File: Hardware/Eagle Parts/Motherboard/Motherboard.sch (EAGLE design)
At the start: 30 parts, among them J1 U.FL, U1 MK10DN512ZVLL10, U4 MPL3115A2LGA8, U5 ATMEGA8U2AU, U6 MPL115A

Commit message: Moved things into separate pages
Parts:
- removed J1: U.FL, SparkFun-Connectors:U.FL
- removed U$10, U$11, U$12, U$13, U$14, U$15, U$3, U$5, U$6, U$7, U$8, U$9: MAX3077, MAX3077:MAX3077
- removed U$24: TB60050685100, harting-scsi:TB60050685100
- removed U2: (no value), adafruit:GPS_FGPMMOPA6H
- removed U3: (no value), SparkFun-Sensors:MPU-9150QFN-24-NP
- removed U4: MPL3115A2LGA8, SparkFun-Sensors:MPL3115A2LGA8
- removed U6: MPL115A, SparkFun-Sensors:MPL115A
- added J2: U.FL, SparkFun-Connectors:U.FL
- added U$25, U$26, U$27, U$28, U$29, U$30, U$31, U$32, U$33, U$34, U$35, U$4: MAX3077, MAX3077:MAX3077
- added U$36: TB60050685100, harting-scsi:TB60050685100
- added U10: MPL115A, SparkFun-Sensors:MPL115A
- added U7: (no value), adafruit:GPS_FGPMMOPA6H
- added U8: (no value), SparkFun-Sensors:MPU-9150QFN-24-NP
- added U9: MPL3115A2LGA8, SparkFun-Sensors:MPL3115A2LGA8
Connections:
- net 10_RX+: now also U$26.A, U$36.39; no longer U$24.39, U$6.A
- net 10_RX-: now also U$26.B, U$36.40; no longer U$24.40, U$6.B
- net 10_TX+: now also U$26.Y, U$36.37; no longer U$24.37, U$6.Y
- net 10_TX-: now also U$26.Z, U$36.38; no longer U$24.38, U$6.Z
- net 11_RX+: now also U$25.A, U$36.43; no longer U$24.43, U$5.A
- net 11_RX-: now also U$25.B, U$36.44; no longer U$24.44, U$5.B
- net 11_TX+: now also U$25.Y, U$36.41; no longer U$24.41, U$5.Y
- net 11_TX-: now also U$25.Z, U$36.42; no longer U$24.42, U$5.Z
- net 12_RX+: now also U$36.47, U$4.A; no longer U$24.47, U$3.A
- net 12_RX-: now also U$36.48, U$4.B; no longer U$24.48, U$3.B
- net 12_TX+: now also U$36.45, U$4.Y; no longer U$24.45, U$3.Y
- net 12_TX-: now also U$36.46, U$4.Z; no longer U$24.46, U$3.Z
- net 1_RX+: now also U$29.A, U$36.3; no longer U$24.3, U$9.A
- net 1_RX-: now also U$29.B, U$36.4; no longer U$24.4, U$9.B
- net 1_TX+: now also U$29.Y, U$36.1; no longer U$24.1, U$9.Y
- net 1_TX-: now also U$29.Z, U$36.2; no longer U$24.2, U$9.Z
- net 2_RX+: now also U$31.A, U$36.7; no longer U$11.A, U$24.7
- net 2_RX-: now also U$31.B, U$36.8; no longer U$11.B, U$24.8
- net 2_TX+: now also U$31.Y, U$36.5; no longer U$11.Y, U$24.5
- net 2_TX-: now also U$31.Z, U$36.6; no longer U$11.Z, U$24.6
- net 3_RX+: now also U$32.A, U$36.11; no longer U$12.A, U$24.11
- net 3_RX-: now also U$32.B, U$36.12; no longer U$12.B, U$24.12
- net 3_TX+: now also U$32.Y, U$36.9; no longer U$12.Y, U$24.9
- net 3_TX-: now also U$32.Z, U$36.10; no longer U$12.Z, U$24.10
- net 4_RX+: now also U$33.A, U$36.15; no longer U$13.A, U$24.15
- net 4_RX-: now also U$33.B, U$36.16; no longer U$13.B, U$24.16
- net 4_TX+: now also U$33.Y, U$36.13; no longer U$13.Y, U$24.13
- net 4_TX-: now also U$33.Z, U$36.14; no longer U$13.Z, U$24.14
- net 5_RX+: now also U$34.A, U$36.19; no longer U$14.A, U$24.19
- net 5_RX-: now also U$34.B, U$36.20; no longer U$14.B, U$24.20
- net 5_TX+: now also U$34.Y, U$36.17; no longer U$14.Y, U$24.17
- net 5_TX-: now also U$34.Z, U$36.18; no longer U$14.Z, U$24.18
- net 6_RX+: now also U$35.A, U$36.23; no longer U$15.A, U$24.23
- net 6_RX-: now also U$35.B, U$36.24; no longer U$15.B, U$24.24
- net 6_TX+: now also U$35.Y, U$36.21; no longer U$15.Y, U$24.21
- net 6_TX-: now also U$35.Z, U$36.22; no longer U$15.Z, U$24.22
- net 7_RX+: now also U$30.A, U$36.27; no longer U$10.A, U$24.27
- net 7_RX-: now also U$30.B, U$36.28; no longer U$10.B, U$24.28
- net 7_TX+: now also U$30.Y, U$36.25; no longer U$10.Y, U$24.25
- net 7_TX-: now also U$30.Z, U$36.26; no longer U$10.Z, U$24.26
- net 8_RX+: now also U$28.A, U$36.31; no longer U$24.31, U$8.A
- net 8_RX-: now also U$28.B, U$36.32; no longer U$24.32, U$8.B
- net 8_TX+: now also U$28.Y, U$36.29; no longer U$24.29, U$8.Y
- net 8_TX-: now also U$28.Z, U$36.30; no longer U$24.30, U$8.Z
- net 9_RX+: now also U$27.A, U$36.35; no longer U$24.35, U$7.A
- net 9_RX-: now also U$27.B, U$36.36; no longer U$24.36, U$7.B
- net 9_TX+: now also U$27.Y, U$36.33; no longer U$24.33, U$7.Y
- net 9_TX-: now also U$27.Z, U$36.34; no longer U$24.34, U$7.Z
- net GND: now also U$25.GND, U$26.GND, U$27.GND, U$28.GND, U$29.GND, U$30.GND, U$31.GND, U$32.GND, U$33.GND, U$34.GND, U$35.GND, U$4.GND; no longer U$10.GND, U$11.GND, U$12.GND, U$13.GND, U$14.GND, U$15.GND, U$3.GND, U$5.GND, U$6.GND, U$7.GND, U$8.GND, U$9.GND

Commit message: Wired Sensor Grounds, Created RS Internal Page
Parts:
- removed U$16, U$17, U$18, U$19, U$20, U$21, U$22, U$23: MAX3077, MAX3077:MAX3077
- added U$10, U$11, U$3, U$5, U$6, U$7, U$8, U$9: MAX3077, MAX3077:MAX3077
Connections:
- net GND: now also U10.GND, U7.GND@1, U7.GND@2, U7.GND@3, U7.GND@4, U8.GND@15, U8.GND@17, U8.GND@18, U9.GND
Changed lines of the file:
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@@
 <part name="U$1" library="w5500_wiznet" deviceset="W5500" device=""/>
 <part name="U$2" library="SPBT2632C2A" deviceset="SPBT2632C2A" device=""/>
-<part name="U$16" library="MAX3077" deviceset="MAX3077" device=""/>
-<part name="U$17" library="MAX3077" deviceset="MAX3077" device=""/>
-<part name="U$18" library="MAX3077" deviceset="MAX3077" device=""/>
-<part name="U$19" library="MAX3077" deviceset="MAX3077" device=""/>
-<part name="U$20" library="MAX3077" deviceset="MAX3077" device=""/>
-<part name="U$21" library="MAX3077" deviceset="MAX3077" device=""/>
-<part name="U$22" library="MAX3077" deviceset="MAX3077" device=""/>
-<part name="U$23" library="MAX3077" deviceset="MAX3077" device=""/>
 <part name="GND1" library="supply1" deviceset="GND" device=""/>
 <part name="U$4" library="MAX3077" deviceset="MAX3077" device=""/>
@@
 <part name="J2" library="SparkFun-Connectors" deviceset="U.FL" device=""/>
 <part name="U10" library="SparkFun-Sensors" deviceset="MPL115A" device=""/>
+<part name="GND2" library="supply1" deviceset="GND" device=""/>
+<part name="GND3" library="supply1" deviceset="GND" device=""/>
+<part name="GND4" library="supply1" deviceset="GND" device=""/>
+<part name="GND5" library="supply1" deviceset="GND" device=""/>
+<part name="GND6" library="supply1" deviceset="GND" device=""/>
+<part name="GND7" library="supply1" deviceset="GND" device=""/>
+<part name="GND8" library="supply1" deviceset="GND" device=""/>
+<part name="U$3" library="MAX3077" deviceset="MAX3077" device=""/>
+<part name="U$5" library="MAX3077" deviceset="MAX3077" device=""/>
+<part name="U$6" library="MAX3077" deviceset="MAX3077" device=""/>
+<part name="U$7" library="MAX3077" deviceset="MAX3077" device=""/>
+<part name="U$8" library="MAX3077" deviceset="MAX3077" device=""/>
+<part name="U$9" library="MAX3077" deviceset="MAX3077" device=""/>
+<part name="U$10" library="MAX3077" deviceset="MAX3077" device=""/>
+<part name="U$11" library="MAX3077" deviceset="MAX3077" device=""/>
 </parts>
 <sheets>
@@
 <text x="-93.98" y="7.62" size="5.08" layer="91">TCP/Eth</text>
 <text x="-91.44" y="-91.44" size="5.08" layer="91">Bluetooth</text>
-<text x="-2.54" y="-63.5" size="5.08" layer="91">RS-485</text>
 </plain>
 <instances>
@@
 <instance part="U$1" gate="G$1" x="-96.52" y="-60.96"/>
 <instance part="U$2" gate="G$1" x="-73.66" y="-116.84"/>
-<instance part="U$16" gate="G$1" x="10.16" y="-76.2"/>
-<instance part="U$17" gate="G$1" x="53.34" y="-73.66"/>
-<instance part="U$18" gate="G$1" x="91.44" y="-73.66"/>
-<instance part="U$19" gate="G$1" x="132.08" y="-73.66"/>
-<instance part="U$20" gate="G$1" x="175.26" y="-71.12"/>
-<instance part="U$21" gate="G$1" x="215.9" y="-71.12"/>
-<instance part="U$22" gate="G$1" x="172.72" y="-114.3"/>
-<instance part="U$23" gate="G$1" x="213.36" y="-114.3"/>
 <instance part="GND1" gate="1" x="-27.94" y="114.3" rot="R270"/>
 </instances>
@@
 </sheet>
 <sheet>
-<description>RS-485</description>
+<description>RS-485 External</description>
 <plain>
 <text x="88.9" y="104.14" size="5.08" layer="91">Ribbon Cable</text>
@@
 </sheet>
 <sheet>
-<description>Sensors</description>
+<description>RS-485 Internal</description>
 <plain>
-<text x="-15.24" y="58.42" size="12.7" layer="91" align="center">GPS</text>
-<text x="35.56" y="58.42" size="12.7" layer="91" align="center">IMU</text>
-<text x="-22.86" y="-17.78" size="5.08" layer="91" align="center">Altimeter</text>
-<text x="5.08" y="-20.32" size="5.08" layer="91">Barometer</text>
+<text x="-116.84" y="30.48" size="5.08" layer="91">RS-485</text>
 </plain>
 <instances>
-<instance part="U7" gate="G$1" x="-20.32" y="20.32"/>
-<instance part="U8" gate="G$1" x="35.56" y="22.86"/>
-<instance part="U9" gate="G$1" x="-20.32" y="-33.02"/>
-<instance part="J2" gate="G$1" x="-50.8" y="38.1"/>
-<instance part="U10" gate="G$1" x="20.32" y="-33.02"/>
+<instance part="U$3" gate="G$1" x="-104.14" y="17.78"/>
+<instance part="U$5" gate="G$1" x="-60.96" y="20.32"/>
+<instance part="U$6" gate="G$1" x="-22.86" y="20.32"/>
+<instance part="U$7" gate="G$1" x="17.78" y="20.32"/>
+<instance part="U$8" gate="G$1" x="60.96" y="22.86"/>
+<instance part="U$9" gate="G$1" x="101.6" y="22.86"/>
+<instance part="U$10" gate="G$1" x="58.42" y="-20.32"/>
+<instance part="U$11" gate="G$1" x="99.06" y="-20.32"/>
 </instances>
 <busses>
@@
 </nets>
 </sheet>
+<sheet>
+<description>Sensors</description>
+<plain>
+<text x="-15.24" y="58.42" size="12.7" layer="91" align="center">GPS</text>
+<text x="63.5" y="50.8" size="12.7" layer="91" align="center">IMU</text>
+<text x="-22.86" y="-17.78" size="5.08" layer="91" align="center">Altimeter</text>
+<text x="48.26" y="-20.32" size="5.08" layer="91">Barometer</text>
+</plain>
+<instances>
+<instance part="U7" gate="G$1" x="-20.32" y="20.32"/>
+<instance part="U8" gate="G$1" x="63.5" y="17.78"/>
+<instance part="U9" gate="G$1" x="-20.32" y="-33.02"/>
+<instance part="J2" gate="G$1" x="-58.42" y="58.42"/>
+<instance part="U10" gate="G$1" x="63.5" y="-33.02"/>
+<instance part="GND2" gate="1" x="43.18" y="-35.56" rot="R270"/>
+<instance part="GND3" gate="1" x="-40.64" y="-35.56" rot="R270"/>
+<instance part="GND4" gate="1" x="-43.18" y="12.7" rot="R270"/>
+<instance part="GND5" gate="1" x="35.56" y="7.62" rot="R270"/>
+<instance part="GND6" gate="1" x="5.08" y="27.94" rot="R90"/>
+<instance part="GND7" gate="1" x="5.08" y="10.16" rot="R90"/>
+<instance part="GND8" gate="1" x="-43.18" y="25.4" rot="R270"/>
+</instances>
+<busses>
+</busses>
+<nets>
+<net name="GND" class="0">
+<segment>
+<pinref part="U8" gate="G$1" pin="GND@18"/>
+<wire x1="45.72" y1="10.16" x2="40.64" y2="10.16" width="0.1524" layer="91"/>
+<wire x1="40.64" y1="10.16" x2="40.64" y2="7.62" width="0.1524" layer="91"/>
+<pinref part="U8" gate="G$1" pin="GND@17"/>
+<wire x1="40.64" y1="7.62" x2="45.72" y2="7.62" width="0.1524" layer="91"/>
+<pinref part="U8" gate="G$1" pin="GND@15"/>
+<wire x1="45.72" y1="5.08" x2="40.64" y2="5.08" width="0.1524" layer="91"/>
+<wire x1="40.64" y1="5.08" x2="40.64" y2="7.62" width="0.1524" layer="91"/>
+<junction x="40.64" y="7.62"/>
+<pinref part="GND5" gate="1" pin="GND"/>
+<wire x1="38.1" y1="7.62" x2="40.64" y2="7.62" width="0.1524" layer="91"/>
+</segment>
+<segment>
+<pinref part="U7" gate="G$1" pin="GND@4"/>
+<pinref part="GND6" gate="1" pin="GND"/>
+<wire x1="-5.08" y1="27.94" x2="2.54" y2="27.94" width="0.1524" layer="91"/>
+</segment>
+<segment>
+<pinref part="GND7" gate="1" pin="GND"/>
+<wire x1="-5.08" y1="10.16" x2="2.54" y2="10.16" width="0.1524" layer="91"/>
+<pinref part="U7" gate="G$1" pin="GND@3"/>
+</segment>
+<segment>
+<pinref part="U7" gate="G$1" pin="GND@2"/>
+<pinref part="GND4" gate="1" pin="GND"/>
+<wire x1="-35.56" y1="12.7" x2="-40.64" y2="12.7" width="0.1524" layer="91"/>
+</segment>
+<segment>
+<pinref part="U10" gate="G$1" pin="GND"/>
+<pinref part="GND2" gate="1" pin="GND"/>
+<wire x1="50.8" y1="-35.56" x2="45.72" y2="-35.56" width="0.1524" layer="91"/>
+</segment>
+<segment>
+<pinref part="U9" gate="G$1" pin="GND"/>
+<pinref part="GND3" gate="1" pin="GND"/>
+<wire x1="-33.02" y1="-35.56" x2="-38.1" y2="-35.56" width="0.1524" layer="91"/>
+</segment>
+<segment>
+<pinref part="GND8" gate="1" pin="GND"/>
+<pinref part="U7" gate="G$1" pin="GND@1"/>
+<wire x1="-40.64" y1="25.4" x2="-35.56" y2="25.4" width="0.1524" layer="91"/>
+</segment>
+</net>
+</nets>
+</sheet>

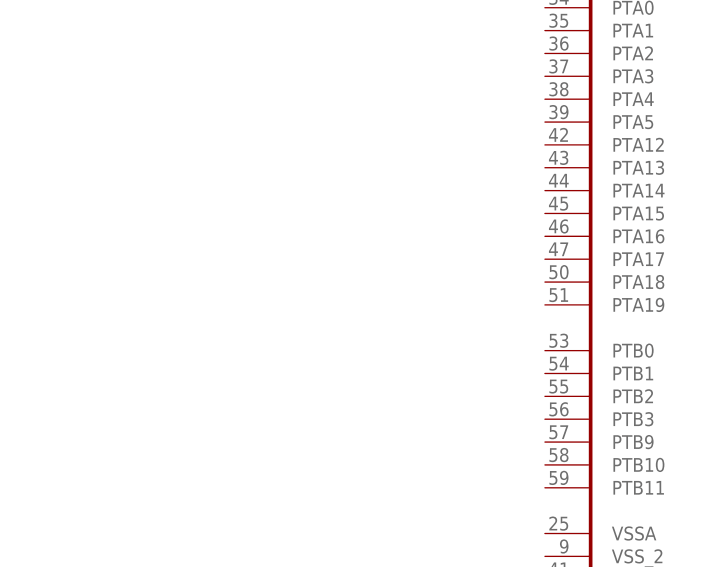
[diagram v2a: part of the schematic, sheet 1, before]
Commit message: Added Xtal to main processor
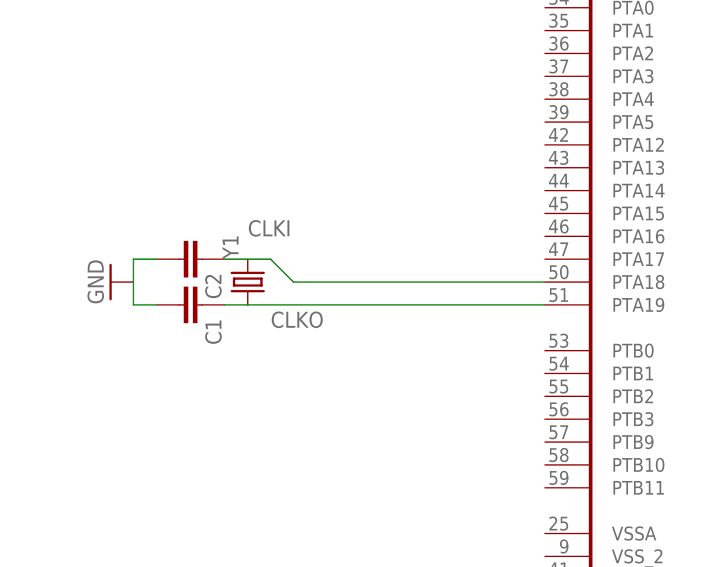
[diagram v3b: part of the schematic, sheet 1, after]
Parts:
- added C1, C2: (no value), SparkFun-Passives:CAPPTH1
- added Y1: (no value), SparkFun-FreqCtrl:CRYSTALHC49US
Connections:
- new net CLKI: C2.1, U1A.PTA18, Y1.2
- new net CLKO: C1.1, U1A.PTA19, Y1.1
- net GND: now also C1.2, C2.2
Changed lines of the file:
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@@
 <part name="U$10" library="MAX3077" deviceset="MAX3077" device=""/>
 <part name="U$11" library="MAX3077" deviceset="MAX3077" device=""/>
+<part name="Y1" library="SparkFun-FreqCtrl" deviceset="CRYSTAL" device="HC49US"/>
+<part name="C1" library="SparkFun-Passives" deviceset="CAP" device="PTH1"/>
+<part name="C2" library="SparkFun-Passives" deviceset="CAP" device="PTH1"/>
+<part name="GND9" library="supply1" deviceset="GND" device=""/>
 </parts>
 <sheets>
@@
 <instance part="U$2" gate="G$1" x="-73.66" y="-116.84"/>
 <instance part="GND1" gate="1" x="-27.94" y="114.3" rot="R270"/>
+<instance part="Y1" gate="G$1" x="-203.2" y="109.22" rot="R90"/>
+<instance part="C1" gate="G$1" x="-210.82" y="106.68" rot="R270"/>
+<instance part="C2" gate="G$1" x="-210.82" y="111.76" rot="R270"/>
+<instance part="GND9" gate="1" x="-218.44" y="109.22" rot="R270"/>
 </instances>
 <busses>
@@
 <wire x1="-20.32" y1="111.76" x2="-20.32" y2="114.3" width="0.1524" layer="91"/>
 </segment>
+<segment>
+<pinref part="C2" gate="G$1" pin="2"/>
+<wire x1="-213.36" y1="111.76" x2="-215.9" y2="111.76" width="0.1524" layer="91"/>
+<pinref part="GND9" gate="1" pin="GND"/>
+<wire x1="-215.9" y1="111.76" x2="-215.9" y2="109.22" width="0.1524" layer="91"/>
+<wire x1="-215.9" y1="109.22" x2="-215.9" y2="106.68" width="0.1524" layer="91"/>
+<pinref part="C1" gate="G$1" pin="2"/>
+<wire x1="-215.9" y1="106.68" x2="-213.36" y2="106.68" width="0.1524" layer="91"/>
+</segment>
 </net>
+<net name="CLKO" class="0">
+<segment>
+<pinref part="Y1" gate="G$1" pin="1"/>
+<pinref part="C1" gate="G$1" pin="1"/>
+<wire x1="-203.2" y1="106.68" x2="-205.74" y2="106.68" width="0.1524" layer="91"/>
+<label x="-200.66" y="104.14" size="1.778" layer="95"/>
+<wire x1="-203.2" y1="106.68" x2="-170.18" y2="106.68" width="0.1524" layer="91"/>
+<pinref part="U1" gate="A" pin="PTA19"/>
+</segment>
+</net>
+<net name="CLKI" class="0">
+<segment>
+<pinref part="Y1" gate="G$1" pin="2"/>
+<pinref part="C2" gate="G$1" pin="1"/>
+<wire x1="-203.2" y1="111.76" x2="-205.74" y2="111.76" width="0.1524" layer="91"/>
+<label x="-203.2" y="114.3" size="1.778" layer="95"/>
+<wire x1="-203.2" y1="111.76" x2="-200.66" y2="111.76" width="0.1524" layer="91"/>
+<wire x1="-200.66" y1="111.76" x2="-198.12" y2="109.22" width="0.1524" layer="91"/>
+<pinref part="U1" gate="A" pin="PTA18"/>
+<wire x1="-198.12" y1="109.22" x2="-170.18" y2="109.22" width="0.1524" layer="91"/>
+</segment>
+</net>
